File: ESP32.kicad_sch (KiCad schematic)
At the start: 6 parts, among them U1 ESP32-C6-MINI-1

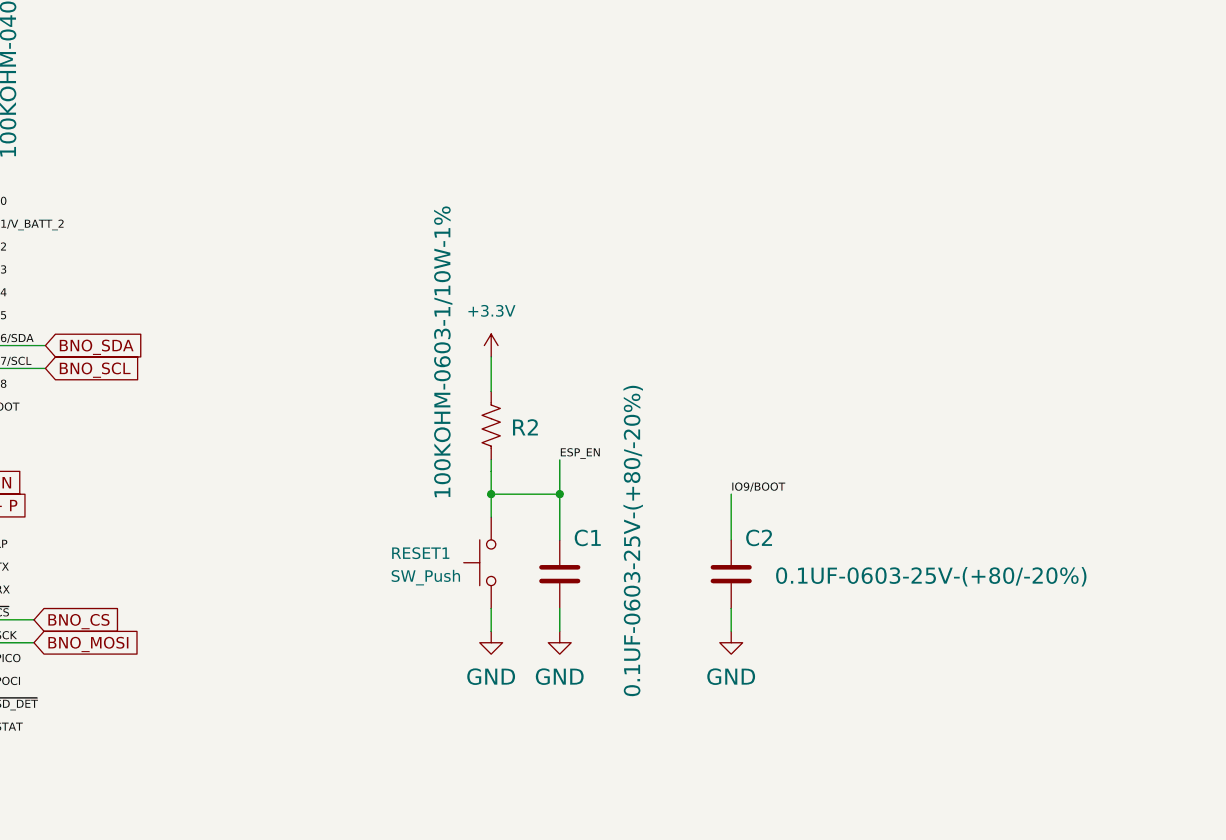
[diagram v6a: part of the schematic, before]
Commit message: Condense schematic
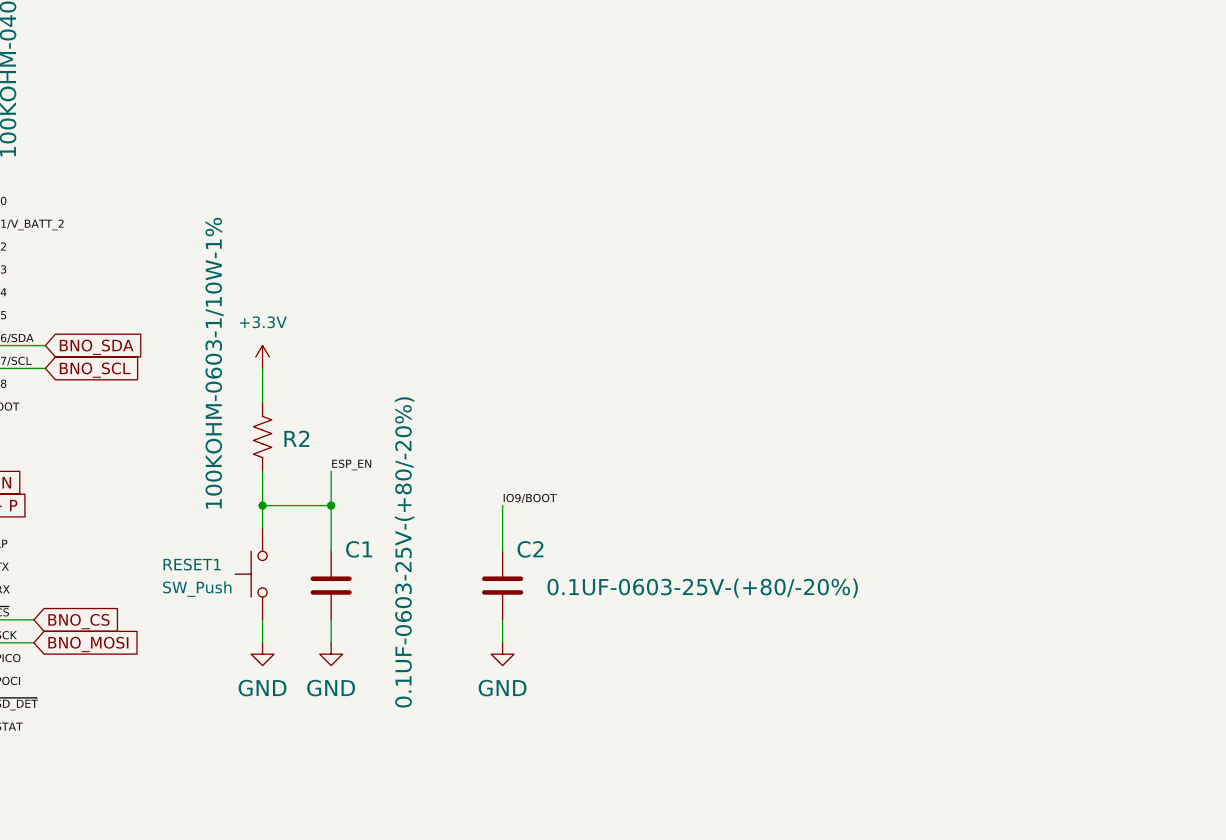
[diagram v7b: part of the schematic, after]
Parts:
- C1, C2: footprint Capacitor_SMD:C_0603_1608Metric -> Capacitor_SMD:C_0402_1005Metric
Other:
- moved on the sheet: C1, C2, R2, RESET1
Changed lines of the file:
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@@
 	)
 	(junction
-		(at 204.47 110.49)
+		(at 179.07 111.76)
 		(diameter 0)
 		(color 0 0 0 0)
 	)
 	(junction
-		(at 196.85 110.49)
+		(at 171.45 111.76)
 		(diameter 0)
 		(color 0 0 0 0)
@@
 	(wire
 		(pts
-			(xy 196.85 113.03) (xy 196.85 110.49)
+			(xy 171.45 114.3) (xy 171.45 111.76)
 		)
 		(stroke
@@
 	(wire
 		(pts
-			(xy 204.47 110.49) (xy 196.85 110.49)
+			(xy 179.07 111.76) (xy 171.45 111.76)
 		)
 		(stroke
@@
 	(wire
 		(pts
-			(xy 223.52 125.73) (xy 223.52 123.19)
+			(xy 198.12 127) (xy 198.12 124.46)
 		)
 		(stroke
@@
 	(wire
 		(pts
-			(xy 204.47 115.57) (xy 204.47 110.49)
+			(xy 179.07 116.84) (xy 179.07 111.76)
 		)
 		(stroke
@@
 	(wire
 		(pts
-			(xy 204.47 125.73) (xy 204.47 123.19)
-		)
-		(stroke
-			(width 0.1524)
-			(type solid)
-		)
-	)
-	(wire
-		(pts
-			(xy 196.85 125.73) (xy 196.85 123.19)
+			(xy 179.07 127) (xy 179.07 124.46)
+		)
+		(stroke
+			(width 0.1524)
+			(type solid)
+		)
+	)
+	(wire
+		(pts
+			(xy 171.45 127) (xy 171.45 124.46)
 		)
 		(stroke
@@
 	(wire
 		(pts
-			(xy 196.85 110.49) (xy 196.85 107.95)
+			(xy 171.45 111.76) (xy 171.45 109.22)
 		)
 		(stroke
@@
 	(wire
 		(pts
-			(xy 196.85 95.25) (xy 196.85 99.06)
-		)
-		(stroke
-			(width 0.1524)
-			(type solid)
-		)
-	)
-	(wire
-		(pts
-			(xy 204.47 106.68) (xy 204.47 110.49)
+			(xy 171.45 96.52) (xy 171.45 100.33)
+		)
+		(stroke
+			(width 0.1524)
+			(type solid)
+		)
+	)
+	(wire
+		(pts
+			(xy 179.07 107.95) (xy 179.07 111.76)
 		)
 		(stroke
@@
 	(wire
 		(pts
-			(xy 223.52 110.49) (xy 223.52 115.57)
+			(xy 198.12 111.76) (xy 198.12 116.84)
 		)
 		(stroke
@@
 	(wire
 		(pts
-			(xy 196.85 106.68) (xy 196.85 107.95)
+			(xy 171.45 107.95) (xy 171.45 109.22)
 		)
 		(stroke
@@
 	)
 	(label "IO9{slash}BOOT"
-		(at 223.52 110.49 0)
+		(at 198.12 111.76 0)
 		(fields_autoplaced yes)
 		(effects
@@
 	)
 	(label "ESP_EN"
-		(at 204.47 106.68 0)
+		(at 179.07 107.95 0)
 		(fields_autoplaced yes)
 		(effects
@@
 	(symbol
 		(lib_id "uSlime:SW_Push")
-		(at 196.85 118.11 90)
+		(at 171.45 119.38 90)
 		(unit 1)
 		(exclude_from_sim no)
@@
 		(dnp no)
 		(property "Reference" "RESET1"
-			(at 185.674 117.094 90)
+			(at 160.274 118.364 90)
 			(effects
 				(font
@@
 		)
 		(property "Value" "SW_Push"
-			(at 185.674 119.634 90)
+			(at 160.274 120.904 90)
 			(effects
 				(font
@@
 		)
 		(property "Footprint" "Button_Switch_SMD:SW_SPST_B3U-1000P-B"
-			(at 191.77 118.11 0)
+			(at 166.37 119.38 0)
 			(effects
 				(font
@@
 		)
 		(property "Datasheet" "~"
-			(at 191.77 118.11 0)
+			(at 166.37 119.38 0)
 			(effects
 				(font
@@
 		)
 		(property "Description" "Push button switch, generic, two pins"
-			(at 196.85 118.11 0)
+			(at 171.45 119.38 0)
 			(effects
 				(font
@@
 	(symbol
 		(lib_id "uSlime:R_US")
-		(at 196.85 102.87 180)
+		(at 171.45 104.14 180)
 		(unit 1)
 		(exclude_from_sim no)
@@
 		(dnp no)
 		(property "Reference" "R2"
-			(at 200.66 102.108 0)
+			(at 175.26 103.378 0)
 			(effects
 				(font
@@
 		)
 		(property "Value" "100KOHM-0603-1/10W-1%"
-			(at 192.532 94.742 90)
+			(at 167.132 96.012 90)
 			(effects
 				(font
@@
 		)
 		(property "Footprint" "Resistor_SMD:R_0402_1005Metric"
-			(at 195.834 102.616 90)
+			(at 170.434 103.886 90)
 			(effects
 				(font
@@
 		)
 		(property "Datasheet" "~"
-			(at 196.85 102.87 0)
+			(at 171.45 104.14 0)
 			(effects
 				(font
@@
 		)
 		(property "Description" "Resistor, US symbol"
-			(at 196.85 102.87 0)
+			(at 171.45 104.14 0)
 			(effects
 				(font
@@
 	(symbol
 		(lib_id "power:GND")
-		(at 196.85 125.73 0)
+		(at 171.45 127 0)
 		(unit 1)
 		(exclude_from_sim no)
@@
 		(dnp no)
 		(property "Reference" "#GND02"
-			(at 196.85 125.73 0)
+			(at 171.45 127 0)
 			(effects
 				(font
@@
 		)
 		(property "Value" "GND"
-			(at 196.85 129.794 0)
+			(at 171.45 131.064 0)
 			(effects
 				(font
@@
 		)
 		(property "Footprint" ""
-			(at 196.85 125.73 0)
+			(at 171.45 127 0)
 			(effects
 				(font
@@
 		)
 		(property "Datasheet" ""
-			(at 196.85 125.73 0)
+			(at 171.45 127 0)
 			(effects
 				(font
@@
 		)
 		(property "Description" "Power symbol creates a global label with name \"GND\" , ground"
-			(at 196.85 125.73 0)
+			(at 171.45 127 0)
 			(effects
 				(font
@@
 	(symbol
 		(lib_id "uSlime:C")
-		(at 204.47 119.38 0)
+		(at 179.07 120.65 0)
 		(unit 1)
 		(exclude_from_sim no)
@@
 		(dnp no)
 		(property "Reference" "C1"
-			(at 205.994 116.459 0)
+			(at 180.594 117.729 0)
 			(effects
 				(font
@@
 		)
 		(property "Value" "0.1UF-0603-25V-(+80/-20%)"
-			(at 213.614 133.096 90)
+			(at 188.214 134.366 90)
 			(effects
 				(font
@@
 			)
 		)
-		(property "Footprint" "Capacitor_SMD:C_0603_1608Metric"
-			(at 205.4352 123.19 0)
+		(property "Footprint" "Capacitor_SMD:C_0402_1005Metric"
+			(at 180.0352 124.46 0)
 			(effects
 				(font
@@
 		)
 		(property "Datasheet" "~"
-			(at 204.47 119.38 0)
+			(at 179.07 120.65 0)
 			(effects
 				(font
@@
 		)
 		(property "Description" "Unpolarized capacitor"
-			(at 204.47 119.38 0)
+			(at 179.07 120.65 0)
 			(effects
 				(font
@@
 	(symbol
 		(lib_id "uSlime:C")
-		(at 223.52 119.38 0)
+		(at 198.12 120.65 0)
 		(unit 1)
 		(exclude_from_sim no)
@@
 		(dnp no)
 		(property "Reference" "C2"
-			(at 225.044 116.459 0)
+			(at 199.644 117.729 0)
 			(effects
 				(font
@@
 		)
 		(property "Value" "0.1UF-0603-25V-(+80/-20%)"
-			(at 228.346 120.65 0)
+			(at 202.946 121.92 0)
 			(effects
 				(font
@@
 			)
 		)
-		(property "Footprint" "Capacitor_SMD:C_0603_1608Metric"
-			(at 224.4852 123.19 0)
+		(property "Footprint" "Capacitor_SMD:C_0402_1005Metric"
+			(at 199.0852 124.46 0)
 			(effects
 				(font
@@
 		)
 		(property "Datasheet" "~"
-			(at 223.52 119.38 0)
+			(at 198.12 120.65 0)
 			(effects
 				(font
@@
 		)
 		(property "Description" "Unpolarized capacitor"
-			(at 223.52 119.38 0)
+			(at 198.12 120.65 0)
 			(effects
 				(font
@@
 	(symbol
 		(lib_id "power:GND")
-		(at 223.52 125.73 0)
+		(at 198.12 127 0)
 		(unit 1)
 		(exclude_from_sim no)
@@
 		(dnp no)
 		(property "Reference" "#GND05"
-			(at 223.52 125.73 0)
+			(at 198.12 127 0)
 			(effects
 				(font
@@
 		)
 		(property "Value" "GND"
-			(at 223.52 129.794 0)
+			(at 198.12 131.064 0)
 			(effects
 				(font
@@
 		)
 		(property "Footprint" ""
-			(at 223.52 125.73 0)
+			(at 198.12 127 0)
 			(effects
 				(font
@@
 		)
 		(property "Datasheet" ""
-			(at 223.52 125.73 0)
+			(at 198.12 127 0)
 			(effects
 				(font
@@
 		)
 		(property "Description" "Power symbol creates a global label with name \"GND\" , ground"
-			(at 223.52 125.73 0)
+			(at 198.12 127 0)
 			(effects
 				(font
@@
 	(symbol
 		(lib_id "power:GND")
-		(at 204.47 125.73 0)
+		(at 179.07 127 0)
 		(unit 1)
 		(exclude_from_sim no)
@@
 		(dnp no)
 		(property "Reference" "#GND03"
-			(at 204.47 125.73 0)
+			(at 179.07 127 0)
 			(effects
 				(font
@@
 		)
 		(property "Value" "GND"
-			(at 204.47 129.794 0)
+			(at 179.07 131.064 0)
 			(effects
 				(font
@@
 		)
 		(property "Footprint" ""
-			(at 204.47 125.73 0)
+			(at 179.07 127 0)
 			(effects
 				(font
@@
 		)
 		(property "Datasheet" ""
-			(at 204.47 125.73 0)
+			(at 179.07 127 0)
 			(effects
 				(font
@@
 		)
 		(property "Description" "Power symbol creates a global label with name \"GND\" , ground"
-			(at 204.47 125.73 0)
+			(at 179.07 127 0)
 			(effects
 				(font
@@
 	(symbol
 		(lib_id "power:+3.3V")
-		(at 196.85 95.25 0)
+		(at 171.45 96.52 0)
 		(unit 1)
 		(exclude_from_sim no)
@@
 		(fields_autoplaced yes)
 		(property "Reference" "#PWR07"
-			(at 196.85 99.06 0)
+			(at 171.45 100.33 0)
 			(effects
 				(font
@@
 		)
 		(property "Value" "+3.3V"
-			(at 196.85 90.17 0)
+			(at 171.45 91.44 0)
 			(effects
 				(font
@@
 		)
 		(property "Footprint" ""
-			(at 196.85 95.25 0)
+			(at 171.45 96.52 0)
 			(effects
 				(font
@@
 		)
 		(property "Datasheet" ""
-			(at 196.85 95.25 0)
+			(at 171.45 96.52 0)
 			(effects
 				(font
@@
 		)
 		(property "Description" "Power symbol creates a global label with name \"+3.3V\""
-			(at 196.85 95.25 0)
-			(effects
-				(font
+			(at 171.45 96.52 0)
+			(effects
+				(font

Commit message: PCB Smol Time
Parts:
- renumbered R6 to R1
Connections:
- net IO2 renamed BNO_INT
- net IO3 renamed BNO_RST
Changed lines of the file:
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@@
 	(wire
 		(pts
-			(xy 135.89 99.06) (xy 138.43 99.06)
-		)
-		(stroke
-			(width 0.1524)
-			(type solid)
-		)
-	)
-	(wire
-		(pts
-			(xy 135.89 91.44) (xy 140.97 91.44)
-		)
-		(stroke
-			(width 0.1524)
-			(type solid)
-		)
-	)
-	(wire
-		(pts
-			(xy 198.12 127) (xy 198.12 124.46)
-		)
-		(stroke
-			(width 0.1524)
-			(type solid)
-		)
-	)
-	(wire
-		(pts
-			(xy 138.43 114.3) (xy 135.89 114.3)
+			(xy 140.97 83.82) (xy 147.32 83.82)
 		)
 		(stroke
@@
 	(wire
 		(pts
+			(xy 135.89 99.06) (xy 138.43 99.06)
+		)
+		(stroke
+			(width 0.1524)
+			(type solid)
+		)
+	)
+	(wire
+		(pts
+			(xy 135.89 91.44) (xy 140.97 91.44)
+		)
+		(stroke
+			(width 0.1524)
+			(type solid)
+		)
+	)
+	(wire
+		(pts
+			(xy 198.12 127) (xy 198.12 124.46)
+		)
+		(stroke
+			(width 0.1524)
+			(type solid)
+		)
+	)
+	(wire
+		(pts
+			(xy 138.43 114.3) (xy 135.89 114.3)
+		)
+		(stroke
+			(width 0)
+			(type default)
+		)
+	)
+	(wire
+		(pts
 			(xy 135.89 83.82) (xy 140.97 83.82)
 		)
@@
 			(width 0.1524)
 			(type solid)
+		)
+	)
+	(wire
+		(pts
+			(xy 140.97 86.36) (xy 147.32 86.36)
+		)
+		(stroke
+			(width 0)
+			(type default)
 		)
 	)
@@
 		)
 	)
+	(global_label "BNO_INT"
+		(shape input)
+		(at 147.32 83.82 0)
+		(fields_autoplaced yes)
+		(effects
+			(font
+				(size 1.27 1.27)
+			)
+			(justify left)
+		)
+		(property "Intersheetrefs" "${INTERSHEET_REFS}"
+			(at 158.1067 83.82 0)
+			(effects
+				(font
+					(size 1.27 1.27)
+				)
+				(justify left)
+				(hide yes)
+			)
+		)
+	)
 	(global_label "D+ P"
 		(shape input)
@@
 		(property "Intersheetrefs" "${INTERSHEET_REFS}"
 			(at 146.5557 109.22 0)
+			(effects
+				(font
+					(size 1.27 1.27)
+				)
+				(justify left)
+				(hide yes)
+			)
+		)
+	)
+	(global_label "BNO_RST"
+		(shape input)
+		(at 147.32 86.36 0)
+		(fields_autoplaced yes)
+		(effects
+			(font
+				(size 1.27 1.27)
+			)
+			(justify left)
+		)
+		(property "Intersheetrefs" "${INTERSHEET_REFS}"
+			(at 158.6509 86.36 0)
 			(effects
 				(font
@@
 		(on_board yes)
 		(dnp no)
-		(property "Reference" "R6"
+		(property "Reference" "R1"
 			(at 138.43 72.644 0)
 			(effects
@@
 			(project "uSlime"
 				(path "/f32c1c49-f803-4e7c-a530-6db148a7ba36/27e9da7b-3bfa-4574-a980-93f02fcd8fa2"
-					(reference "R6")
+					(reference "R1")
 					(unit 1)
 				)
